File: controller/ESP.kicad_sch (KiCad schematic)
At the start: 6 parts

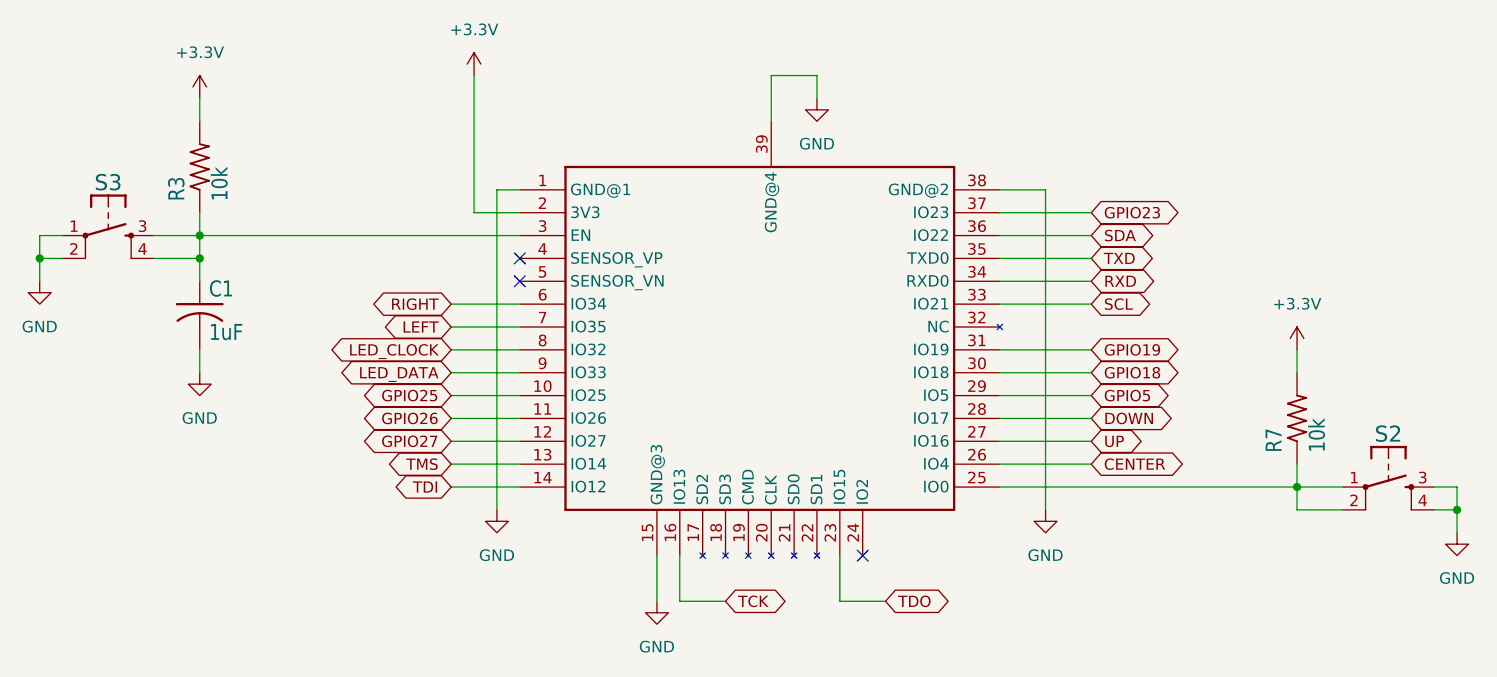
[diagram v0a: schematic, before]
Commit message: Cleaned up controller
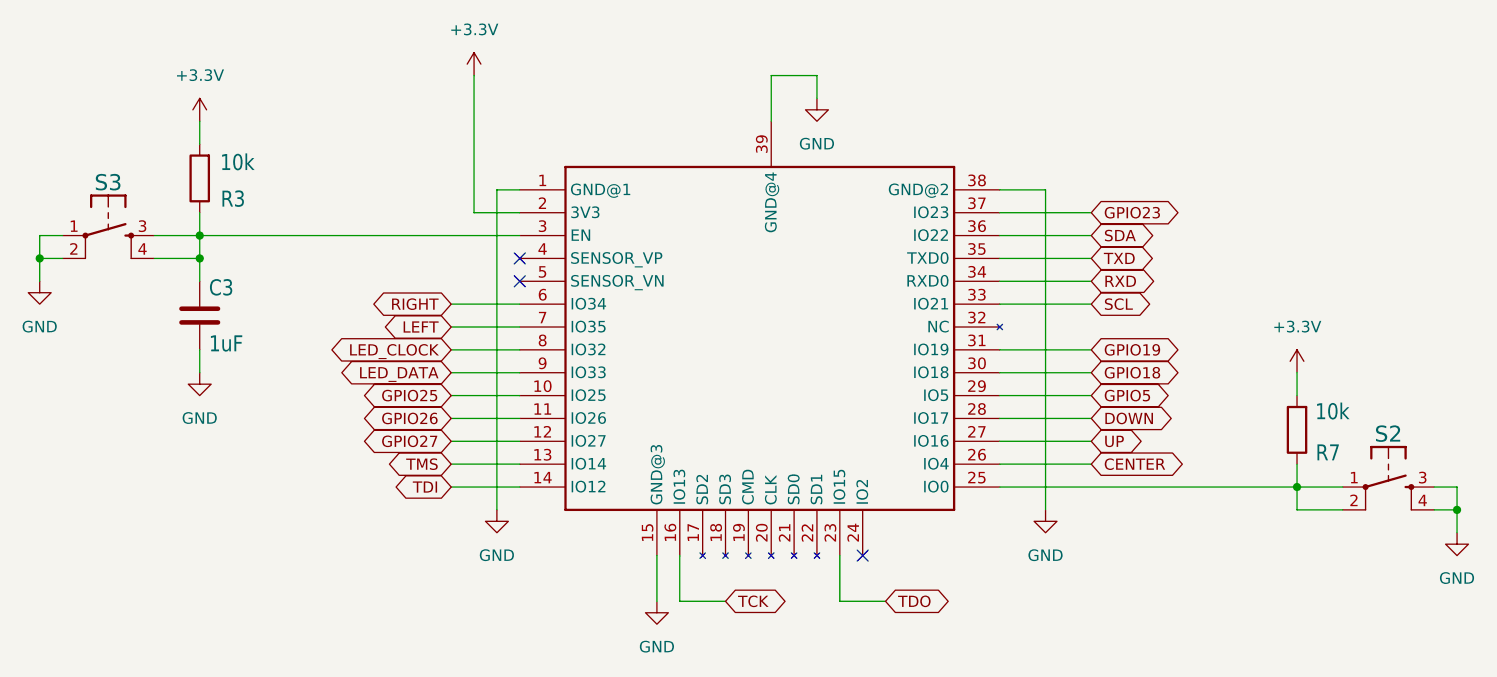
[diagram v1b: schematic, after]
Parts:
- C3: renamed from C1; symbol controller-eagle-import:C-USC0805 -> Device:C
- R3, R7: symbol controller-eagle-import:R-US_R0805 -> Device:R
- S2, S3: symbol controller-eagle-import:MOMENTARY-SWITCH-SPST-2-SMD-4.6X2.8MM -> controller:MOMENTARY-SWITCH-SPST-2-SMD-4.6X2.8MM
- U$2: symbol controller-eagle-import:ESP32-WROOM-32D -> controller:ESP32-WROOM-32D
